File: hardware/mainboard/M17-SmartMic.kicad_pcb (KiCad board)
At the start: 4 copper layers, 99.5 x 80 mm, 204 parts, among them IC301 LM4991MA, J301 CAT_TX, J302 CAT_RX, J401 Radio, J402 USB_C, J403 Radio_Opt, J404 Kenwood-3.5, J405 Kenwood-2.5, J406 2.54mm Header 7p, J407 KH-RJ45-58-8P8C, J408 STLink, J409 UART, J410 Speaker, J411 +12V, J412 Hirose FH12-26S-0.5SH(55), J413 Molex 532610271, Q201 MMBT3904, Q202 IRLML2244, Q301 IRLML2060, Q302 BSS138, Q303 BSS138, SW201 Tactile switch, SW202 Tactile switch, SW203 Tactile switch, SW204 Tactile switch, SW205 Tactile switch, SW206 Tactile switch, SW207 Tactile switch, SW208 Tactile switch, U201 STM32F405RGTx, U202 TPS7A2033, U203 TP6841S6, U301 MCP6002, U302 MAX9814, U401 USBLC6-2SC6, U501 MCP4551-103, U502 MCP4551-103, U503 MCP6002, U504 MCP6002, Y201 8 MHz

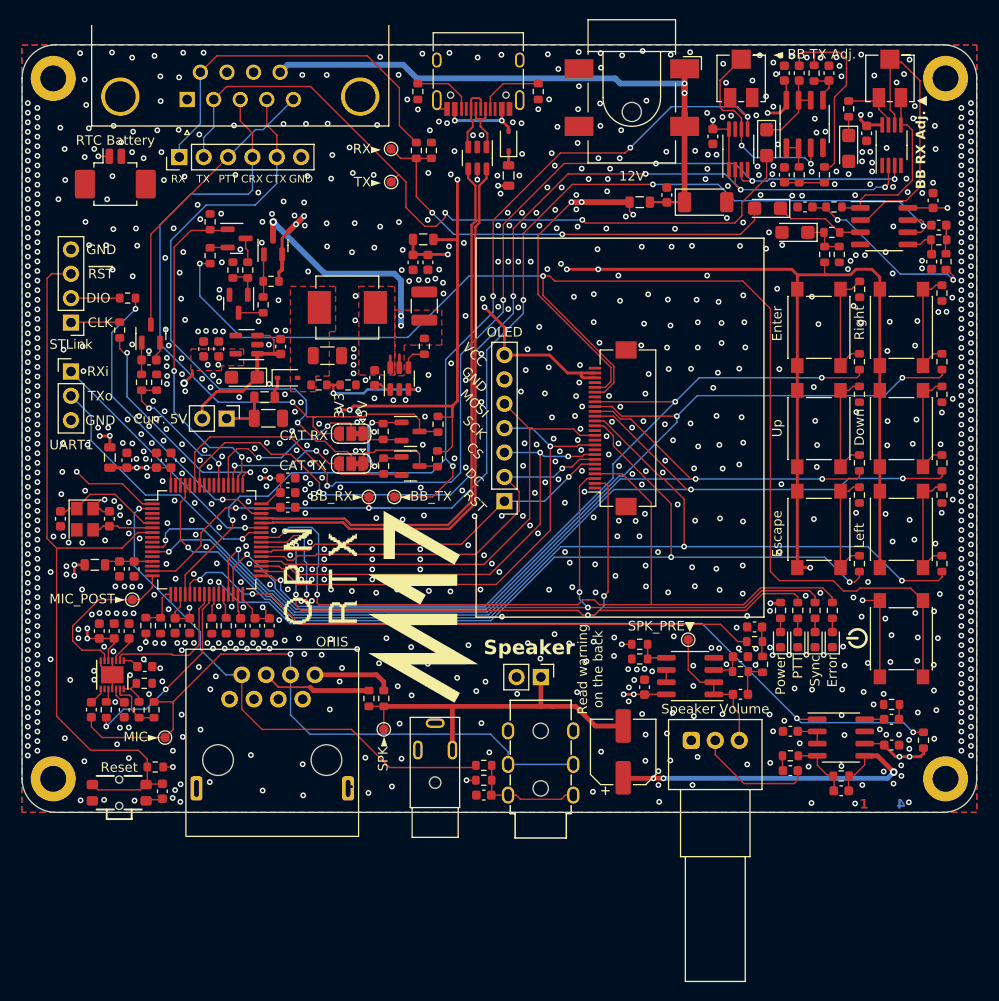
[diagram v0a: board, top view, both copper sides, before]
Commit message: Made the board 0.5mm wider
Effectively reverting commit ef7688b10c0facac2c1ed25a8adbc8398abe4afe.
The 99.5mm board has a bit of play in the enclosure. Making it 100mm will make the fit snug.
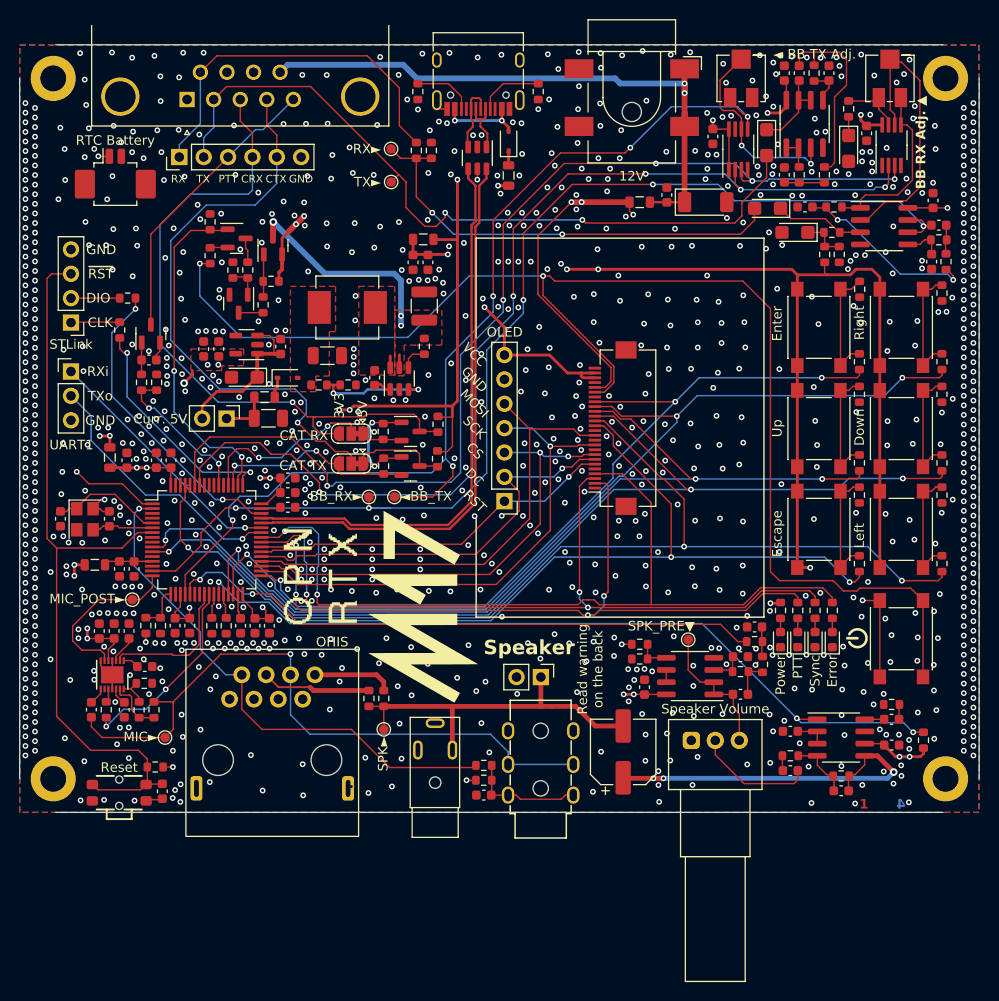
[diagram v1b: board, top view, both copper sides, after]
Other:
- board size 99.5 x 80 mm -> 100 x 80 mm
